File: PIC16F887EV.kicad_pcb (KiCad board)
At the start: 2 copper layers, 100 x 100 mm, 85 parts, among them J1 Conn_01x05_Socket, P1 USB_C_Plug_USB2.0, Q1 2N3904, Q2 2N3904, Q3 2N3904, Q5 2N3904, SW1 SW_Push, SW10 SW_Push, SW11 SW_Push, SW12 SW_Push, SW13 SW_Push, SW14 SW_Push, SW15 SW_Push, SW16 SW_Push, SW17 SW_Push, SW18 SW_Push, SW2 SW_Push, SW3 SW_Push, SW4 SW_Push, SW5 SW_Push, SW6 SW_Push, SW7 SW_Push, SW8 SW_Push, SW9 SW_Push, U1 PIC16F887-IP, U2 FT230XS, Y1 Crystal

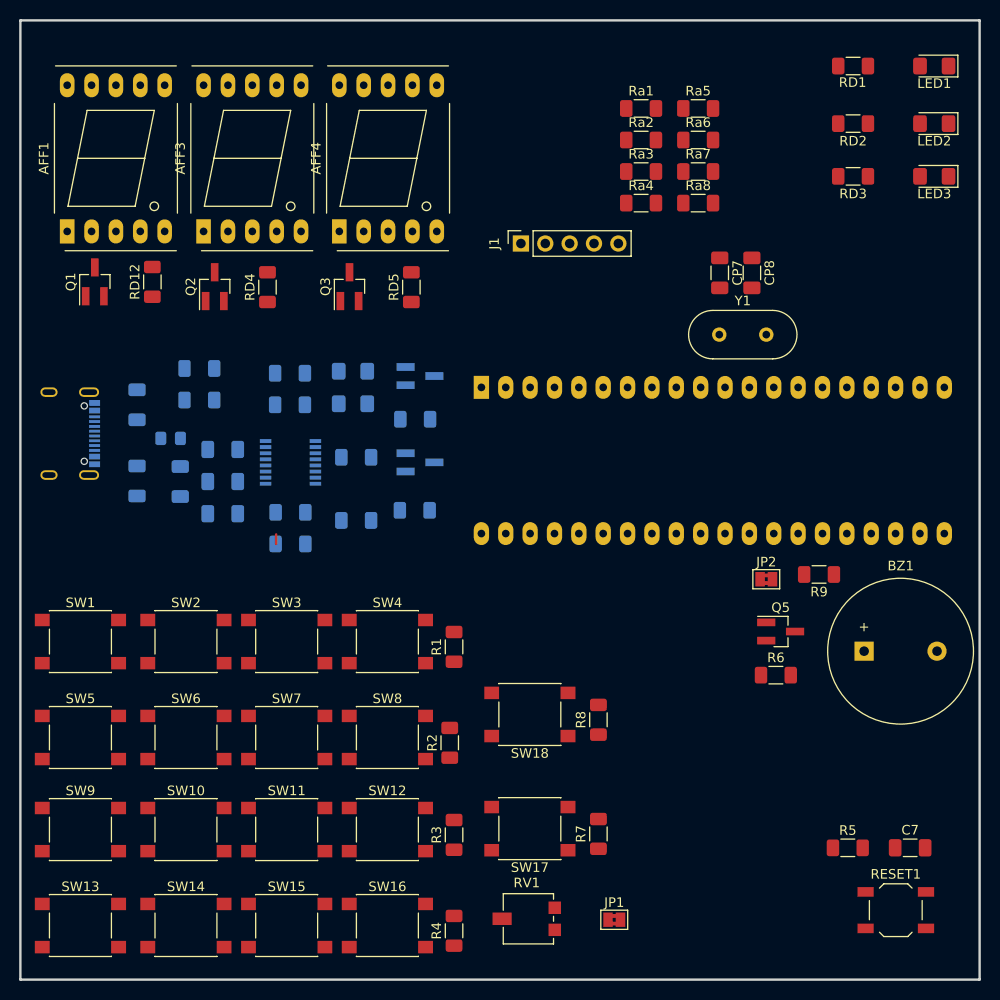
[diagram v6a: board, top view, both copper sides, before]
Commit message: Tornillos + Huella Potenciometro
Agregado de 4 huecos para tornillos de montaje
Cambio de huella del potenciómetro
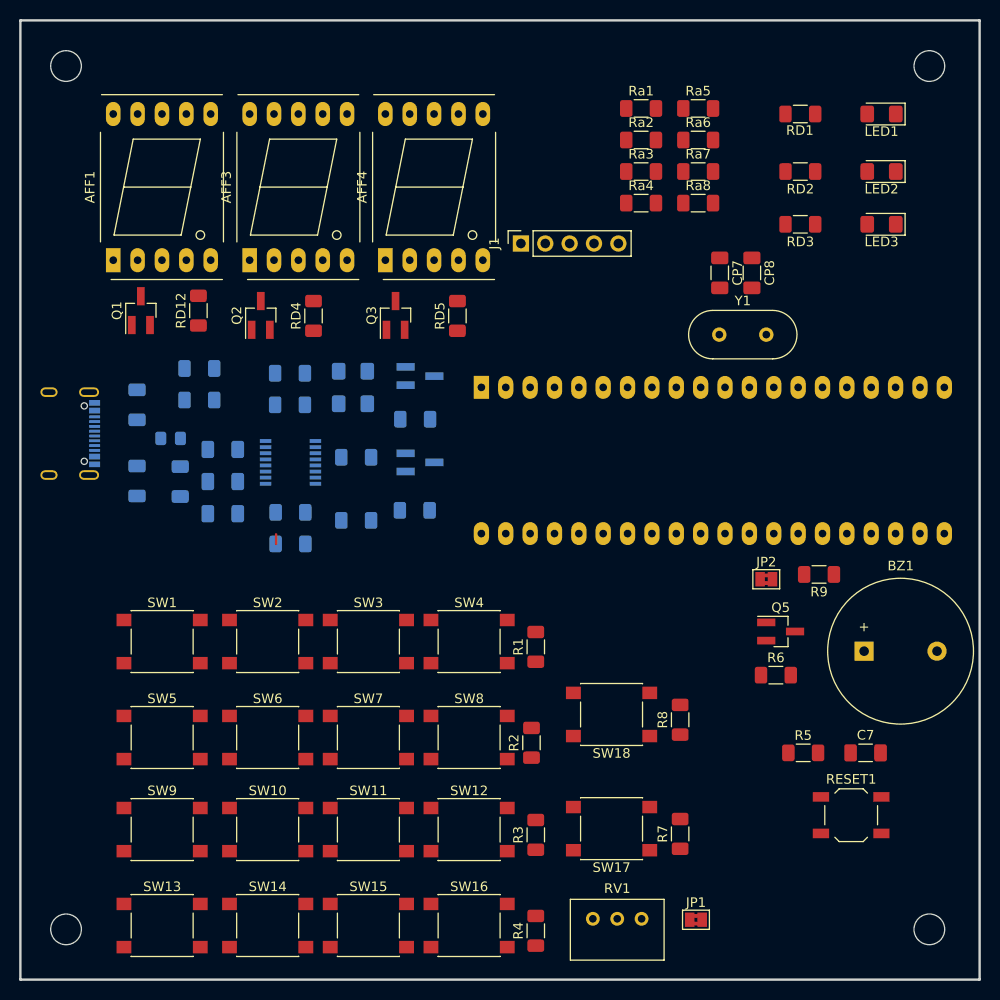
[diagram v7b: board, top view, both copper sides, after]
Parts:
- added REF1: MountingHole_3.2mm_M3, MountingHole:MountingHole_3.2mm_M3, F.Cu at (20.0, 20.0)
- added REF2: MountingHole_3.2mm_M3, MountingHole:MountingHole_3.2mm_M3, F.Cu at (110.0, 20.0)
- added REF3: MountingHole_3.2mm_M3, MountingHole:MountingHole_3.2mm_M3, F.Cu at (20.0, 110.0)
- added REF4: MountingHole_3.2mm_M3, MountingHole:MountingHole_3.2mm_M3, F.Cu at (110.0, 110.0)
- RV1: footprint Potentiometer_SMD:Potentiometer_Vishay_TS53YL_Vertical -> Potentiometer_THT:Potentiometer_Bourns_3299W_Vertical
- moved RV1 11.8 mm to (80.0, 108.9)
- moved C7 10.9 mm to (103.3, 91.6)
- moved R5 10.9 mm to (96.8, 91.6)
- moved RESET1 10.9 mm to (101.8, 98.1)
- moved SW17 8.52 mm to (76.9, 99.5)
- moved SW18 8.52 mm to (76.9, 87.6)
- moved SW10 8.52 mm to (41.0, 99.6)
- moved SW11 8.52 mm to (51.5, 99.6)
- moved SW12 8.52 mm to (62.0, 99.6)
- moved SW14 8.52 mm to (41.0, 109.6)
- moved SW15 8.52 mm to (51.5, 109.6)
- moved SW16 8.52 mm to (62.0, 109.6)
- moved SW2 8.52 mm to (41.0, 80.0)
- moved SW3 8.52 mm to (51.5, 80.0)
- moved SW4 8.52 mm to (62.0, 80.0)
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
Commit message: Ruteo provisorio capa frontal
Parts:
- Q1, Q2, Q3, RD12, RD4, RD5, Ra1, Ra2, Ra3, Ra4, Ra5, Ra6, Ra7, Ra8: moved to B.Cu
- moved RESET1 93.2 mm to (22.0, 50.0)
- moved P1 91.3 mm to (110.5, 62.2), turned to -90 degrees
- moved CP2 88.0 mm to (104.8, 97.1), turned to -90 degrees
- moved C7 82.2 mm to (29.2, 56.0), turned to -90 degrees
- moved CP3 81.7 mm to (104.8, 89.2), turned to 90 degrees
- moved RP1 81.2 mm to (98.3, 100.9), turned to 180 degrees
- moved RV1 80.0 mm to (93.0, 30.0), turned to 90 degrees
- moved FB1 78.6 mm to (101.3, 93.6), turned to 180 degrees
- moved RP2 77.4 mm to (98.3, 97.6), turned to 180 degrees
- moved CP1 73.1 mm to (100.3, 89.1), turned to -90 degrees
- moved R5 72.2 mm to (34.0, 56.0), turned to 90 degrees
- moved JP1 68.6 mm to (92.0, 40.6), turned to -90 degrees
- moved CP6 67.9 mm to (95.9, 92.5), turned to 180 degrees
- moved RP4 66.4 mm to (88.9, 100.4), turned to 180 degrees
- moved CP5 64.9 mm to (95.9, 89.1), turned to 180 degrees
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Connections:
- SW10 pad 2: unconnected-(SW10-Pad2) -> RB2
- SW11 pad 2: unconnected-(SW11-Pad2) -> RB2
- SW12 pad 2: unconnected-(SW12-Pad2) -> RB2
- SW9 pad 2: unconnected-(SW9-Pad2) -> RB2
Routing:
- net +5V: track 0.00 -> 224.4 mm
- net RB3: track 0.00 -> 99.1 mm
- net RB2: track 0.00 -> 91.0 mm
- net RB1: track 0.00 -> 79.0 mm
- net RB0: track 0.00 -> 72.8 mm
- net RB4: track 0.00 -> 53.3 mm
- net RA5: track 0.00 -> 42.6 mm
- net RB5: track 0.00 -> 33.8 mm
- net RA1: track 0.00 -> 31.8 mm
- net RA3: track 0.00 -> 31.8 mm
- net RA2: track 0.00 -> 31.8 mm
- net RA0: track 0.00 -> 31.8 mm
- net RC2: track 0.00 -> 24.8 mm
- net RC1: track 0.00 -> 24.6 mm
- net MCLR: track 0.00 -> 24.6 mm
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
